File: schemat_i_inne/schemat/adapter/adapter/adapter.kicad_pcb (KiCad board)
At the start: 2 copper layers, 27.9 x 19 mm, 2 parts, among them J1 Conn_01x06_Female, J2 RJ45

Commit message: Upraszczanie polaczen i poprawianie plytki
Gotowe polaczenia do ekranu
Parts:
- added C1: C, Connector_PinHeader_2.54mm:PinHeader_1x02_P2.54mm_Vertical, F.Cu at (34.3, 20.3)
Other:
- board size 27.9 x 19 mm -> 186.7 x 274.3 mm
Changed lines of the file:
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@@
   (general
     (thickness 1.6)
-    (drawings 4)
+    (drawings 6)
     (tracks 12)
     (zones 0)
-    (modules 2)
+    (modules 3)
     (nets 9)
   )
-  (page A4)
+  (page A4 portrait)
   (layers
     (0 F.Cu signal)
@@
   )
   (setup
-    (last_trace_width 0.5)
+    (last_trace_width 0.25)
     (user_trace_width 0.5)
     (user_trace_width 1)
@@
   (net 3 "Net-(J1-Pad4)")
   (net 4 "Net-(J1-Pad3)")
-  (net 5 "Net-(J1-Pad2)")
-  (net 6 "Net-(J1-Pad1)")
-  (net 7 "Net-(J2-Pad8)")
-  (net 8 "Net-(J2-Pad7)")
+  (net 5 "Net-(J2-Pad8)")
+  (net 6 "Net-(J2-Pad7)")
+  (net 7 "Net-(C1-Pad2)")
+  (net 8 "Net-(C1-Pad1)")
   (net_class Default "To jest domyślna klasa połączeń."
     (clearance 0.2)
@@
     (uvia_dia 0.3)
     (uvia_drill 0.1)
-    (add_net "Net-(J1-Pad1)")
-    (add_net "Net-(J1-Pad2)")
+    (add_net "Net-(C1-Pad1)")
+    (add_net "Net-(C1-Pad2)")
     (add_net "Net-(J1-Pad3)")
     (add_net "Net-(J1-Pad4)")
@@
     (add_net "Net-(J2-Pad7)")
     (add_net "Net-(J2-Pad8)")
+  )
+  (module Connector_PinHeader_2.54mm:PinHeader_1x02_P2.54mm_Vertical (layer F.Cu)
+    (at 34.29 20.32)
+    (descr "Through hole straight pin header, 1x02, 2.54mm pitch, single row")
+    (tags "Through hole pin header THT 1x02 2.54mm single row")
+    (fp_text reference C1 (at 0 -2.33) (layer F.SilkS)
+      (effects (font (size 1 1) (thickness 0.15)))
+    )
+    (fp_text value C (at 0 4.87) (layer F.Fab)
+      (effects (font (size 1 1) (thickness 0.15)))
+    )
+    (fp_text user %R (at 0 1.27 90) (layer F.Fab)
+      (effects (font (size 1 1) (thickness 0.15)))
+    )
+    (fp_line (start 1.8 -1.8) (end -1.8 -1.8) (layer F.CrtYd) (width 0.05))
+    (fp_line (start 1.8 4.35) (end 1.8 -1.8) (layer F.CrtYd) (width 0.05))
+    (fp_line (start -1.8 4.35) (end 1.8 4.35) (layer F.CrtYd) (width 0.05))
+    (fp_line (start -1.8 -1.8) (end -1.8 4.35) (layer F.CrtYd) (width 0.05))
+    (fp_line (start -1.33 -1.33) (end 0 -1.33) (layer F.SilkS) (width 0.12))
+    (fp_line (start -1.33 0) (end -1.33 -1.33) (layer F.SilkS) (width 0.12))
+    (fp_line (start -1.33 1.27) (end 1.33 1.27) (layer F.SilkS) (width 0.12))
+    (fp_line (start 1.33 1.27) (end 1.33 3.87) (layer F.SilkS) (width 0.12))
+    (fp_line (start -1.33 1.27) (end -1.33 3.87) (layer F.SilkS) (width 0.12))
+    (fp_line (start -1.33 3.87) (end 1.33 3.87) (layer F.SilkS) (width 0.12))
+    (fp_line (start -1.27 -0.635) (end -0.635 -1.27) (layer F.Fab) (width 0.1))
+    (fp_line (start -1.27 3.81) (end -1.27 -0.635) (layer F.Fab) (width 0.1))
+    (fp_line (start 1.27 3.81) (end -1.27 3.81) (layer F.Fab) (width 0.1))
+    (fp_line (start 1.27 -1.27) (end 1.27 3.81) (layer F.Fab) (width 0.1))
+    (fp_line (start -0.635 -1.27) (end 1.27 -1.27) (layer F.Fab) (width 0.1))
+    (pad 2 thru_hole oval (at 0 2.54) (size 1.7 1.7) (drill 1) (layers *.Cu *.Mask)
+      (net 7 "Net-(C1-Pad2)"))
+    (pad 1 thru_hole rect (at 0 0) (size 1.7 1.7) (drill 1) (layers *.Cu *.Mask)
+      (net 8 "Net-(C1-Pad1)"))
+    (model ${KISYS3DMOD}/Connector_PinHeader_2.54mm.3dshapes/PinHeader_1x02_P2.54mm_Vertical.wrl
+      (at (xyz 0 0 0))
+      (scale (xyz 1 1 1))
+      (rotate (xyz 0 0 0))
+    )
   )
   (module Connector_RJ:RJ45_Amphenol_54602-x08_Horizontal (layer F.Cu)
@@
     )
     (pad 8 thru_hole circle (at 8.89 -2.54 270) (size 1.5 1.5) (drill 0.76) (layers *.Cu *.Mask)
-      (net 7 "Net-(J2-Pad8)"))
+      (net 5 "Net-(J2-Pad8)"))
     (pad 7 thru_hole circle (at 7.62 0 270) (size 1.5 1.5) (drill 0.76) (layers *.Cu *.Mask)
-      (net 8 "Net-(J2-Pad7)"))
+      (net 6 "Net-(J2-Pad7)"))
     (pad 6 thru_hole circle (at 6.35 -2.54 270) (size 1.5 1.5) (drill 0.76) (layers *.Cu *.Mask)
       (net 1 "Net-(J1-Pad6)"))
@@
       (net 4 "Net-(J1-Pad3)"))
     (pad 2 thru_hole circle (at 1.27 -2.54 270) (size 1.5 1.5) (drill 0.76) (layers *.Cu *.Mask)
-      (net 5 "Net-(J1-Pad2)"))
+      (net 7 "Net-(C1-Pad2)"))
     (pad 1 thru_hole rect (at 0 0 270) (size 1.5 1.5) (drill 0.76) (layers *.Cu *.Mask)
-      (net 6 "Net-(J1-Pad1)"))
+      (net 8 "Net-(C1-Pad1)"))
     (pad "" np_thru_hole circle (at -1.27 6.35 270) (size 3.2 3.2) (drill 3.2) (layers *.Cu *.Mask))
     (pad "" np_thru_hole circle (at 10.16 6.35 270) (size 3.2 3.2) (drill 3.2) (layers *.Cu *.Mask))
@@
       (net 4 "Net-(J1-Pad3)"))
     (pad 2 thru_hole oval (at 0 2.54) (size 1.7 1.7) (drill 1) (layers *.Cu *.Mask)
-      (net 5 "Net-(J1-Pad2)"))
+      (net 7 "Net-(C1-Pad2)"))
     (pad 1 thru_hole rect (at 0 0) (size 1.7 1.7) (drill 1) (layers *.Cu *.Mask)
-      (net 6 "Net-(J1-Pad1)"))
+      (net 8 "Net-(C1-Pad1)"))
     (model ${KISYS3DMOD}/Connector_PinHeader_2.54mm.3dshapes/PinHeader_1x06_P2.54mm_Vertical.wrl
       (at (xyz 0 0 0))
@@
     )
   )
-  (gr_line (start 40.64 17.78) (end 12.7 17.78) (layer Edge.Cuts) (width 0.05))
-  (gr_line (start 40.64 36.83) (end 40.64 17.78) (layer Edge.Cuts) (width 0.05))
-  (gr_line (start 12.7 36.83) (end 40.64 36.83) (layer Edge.Cuts) (width 0.05))
-  (gr_line (start 12.7 17.78) (end 12.7 36.83) (layer Edge.Cuts) (width 0.05))
+  (dimension 19.05 (width 0.12) (layer F.SilkS)
+    (gr_text "19,050 mm" (at 44.45 27.305 270) (layer F.SilkS)
+      (effects (font (size 1 1) (thickness 0.15)))
+    )
+    (feature1 (pts (xy 40.64 36.83) (xy 43.766421 36.83)))
+    (feature2 (pts (xy 40.64 17.78) (xy 43.766421 17.78)))
+    (crossbar (pts (xy 43.18 17.78) (xy 43.18 36.83)))
+    (arrow1a (pts (xy 43.18 36.83) (xy 42.593579 35.703496)))
+    (arrow1b (pts (xy 43.18 36.83) (xy 43.766421 35.703496)))
+    (arrow2a (pts (xy 43.18 17.78) (xy 42.593579 18.906504)))
+    (arrow2b (pts (xy 43.18 17.78) (xy 43.766421 18.906504)))
+  )
+  (dimension 27.94 (width 0.12) (layer F.SilkS)
+    (gr_text "27,940 mm" (at 26.67 15.24) (layer F.SilkS)
+      (effects (font (size 1 1) (thickness 0.15)))
+    )
+    (feature1 (pts (xy 40.64 17.78) (xy 40.64 15.923579)))
+    (feature2 (pts (xy 12.7 17.78) (xy 12.7 15.923579)))
+    (crossbar (pts (xy 12.7 16.51) (xy 40.64 16.51)))
+    (arrow1a (pts (xy 40.64 16.51) (xy 39.513496 17.096421)))
+    (arrow1b (pts (xy 40.64 16.51) (xy 39.513496 15.923579)))
+    (arrow2a (pts (xy 12.7 16.51) (xy 13.826504 17.096421)))
+    (arrow2b (pts (xy 12.7 16.51) (xy 13.826504 15.923579)))
+  )
+  (gr_line (start 11.43 285.75) (end 11.43 11.43) (layer Edge.Cuts) (width 0.05))
+  (gr_line (start 198.12 285.75) (end 11.43 285.75) (layer Edge.Cuts) (width 0.05))
+  (gr_line (start 198.12 11.43) (end 198.12 285.75) (layer Edge.Cuts) (width 0.05))
+  (gr_line (start 11.43 11.43) (end 198.12 11.43) (layer Edge.Cuts) (width 0.05))
   (segment (start 34.29 29.21) (end 38.1 33.02) (width 0.25) (layer F.Cu) (net 1))
   (segment (start 30.48 29.21) (end 34.29 29.21) (width 0.25) (layer F.Cu) (net 1))
@@
   (segment (start 30.48 26.67) (end 36.83 26.67) (width 0.25) (layer F.Cu) (net 3))
   (segment (start 27.94 25.4) (end 38.1 25.4) (width 0.25) (layer F.Cu) (net 4))
-  (segment (start 31.75 22.86) (end 30.48 24.13) (width 0.5) (layer F.Cu) (net 5))
-  (segment (start 38.1 22.86) (end 31.75 22.86) (width 0.5) (layer F.Cu) (net 5))
-  (segment (start 27.94 21.61) (end 27.94 22.86) (width 0.5) (layer F.Cu) (net 6))
-  (segment (start 29.23 20.32) (end 27.94 21.61) (width 0.5) (layer F.Cu) (net 6))
-  (segment (start 38.1 20.32) (end 29.23 20.32) (width 0.5) (layer F.Cu) (net 6))
-  (zone (net 5) (net_name "Net-(J1-Pad2)") (layer F.Cu) (hatch edge 0.508)
+  (segment (start 31.75 22.86) (end 30.48 24.13) (width 0.5) (layer F.Cu) (net 7))
+  (segment (start 38.1 22.86) (end 31.75 22.86) (width 0.5) (layer F.Cu) (net 7))
+  (segment (start 27.94 21.61) (end 27.94 22.86) (width 0.5) (layer F.Cu) (net 8))
+  (segment (start 29.23 20.32) (end 27.94 21.61) (width 0.5) (layer F.Cu) (net 8))
+  (segment (start 38.1 20.32) (end 29.23 20.32) (width 0.5) (layer F.Cu) (net 8))
+  (zone (net 7) (net_name "Net-(C1-Pad2)") (layer F.Cu) (hatch edge 0.508)
     (connect_pads yes (clearance 0.508))
     (min_thickness 0.254)

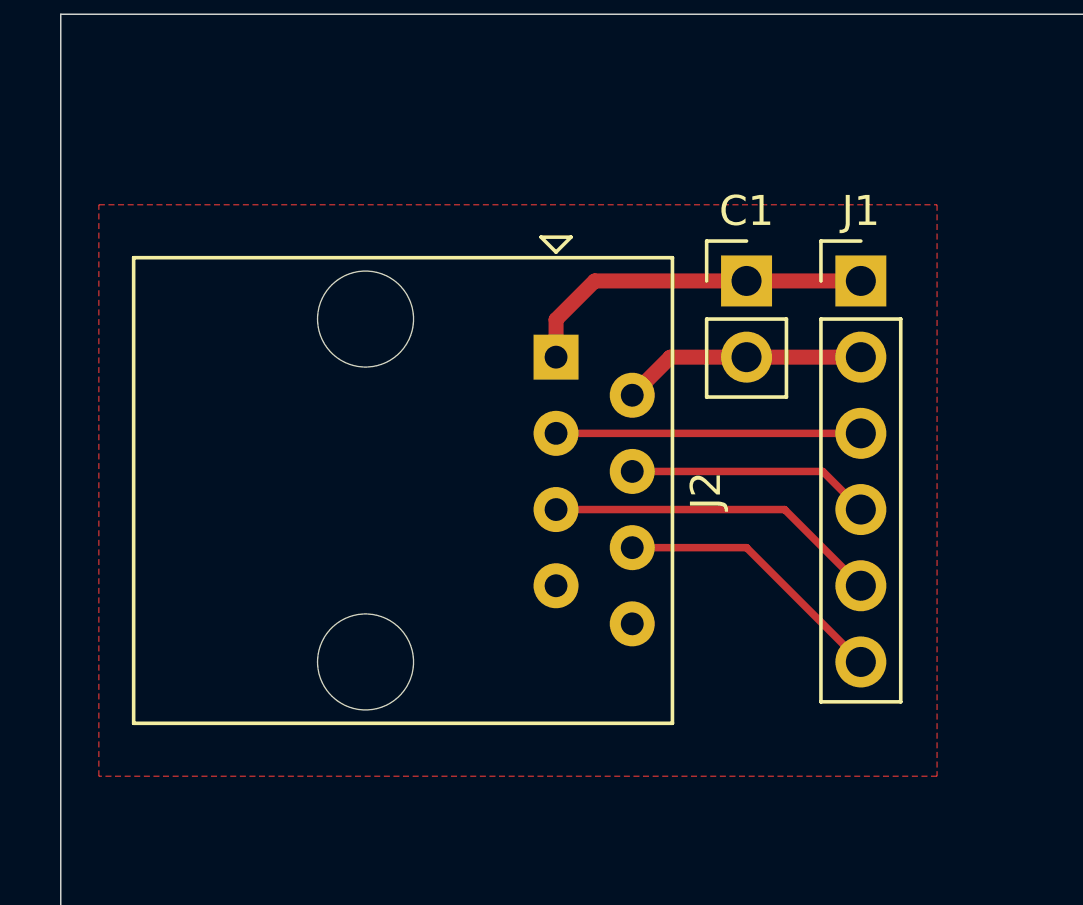
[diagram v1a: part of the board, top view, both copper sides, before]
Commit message: Koncowe sciezki i adapter
Ukonczono poprawianie sciezek i poprawnie zrobiono adapter
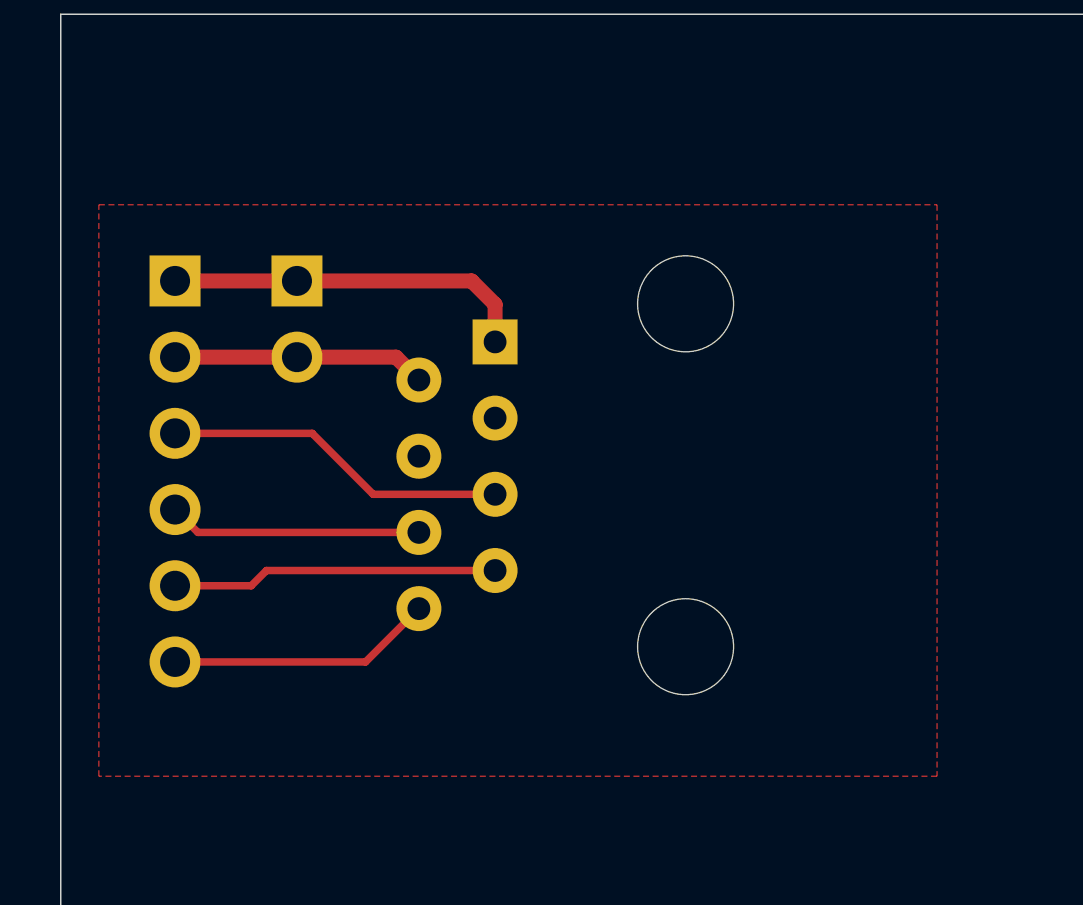
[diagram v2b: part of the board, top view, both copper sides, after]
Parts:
- C1, J1, J2: moved to B.Cu
- moved J1 22.9 mm to (15.2, 20.3), turned to 180 degrees
- moved C1 15.0 mm to (19.3, 20.3), turned to 180 degrees
- moved J2 2.09 mm to (25.9, 22.4)
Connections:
- J2 pad 3: Net-(J1-Pad3) -> Net-(J2-Pad3)
- J2 pad 4: Net-(J1-Pad4) -> Net-(J2-Pad4)
- J2 pad 5: Net-(J1-Pad5) -> Net-(J1-Pad3)
- J2 pad 6: Net-(J1-Pad6) -> Net-(J1-Pad4)
- J2 pad 7: Net-(J2-Pad7) -> Net-(J1-Pad5)
- J2 pad 8: Net-(J2-Pad8) -> Net-(J1-Pad6)
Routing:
- net Net-(J1-Pad3): track 10.2 -> 11.5 mm

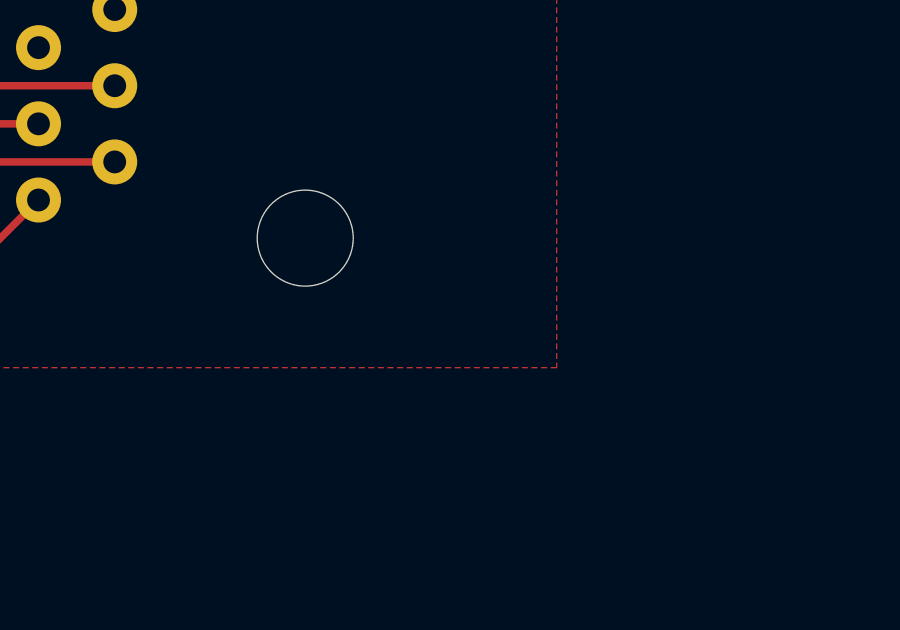
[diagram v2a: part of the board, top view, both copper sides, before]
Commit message: Logo i wymiary
Dodano "by KK" i wymiary plyty glownej
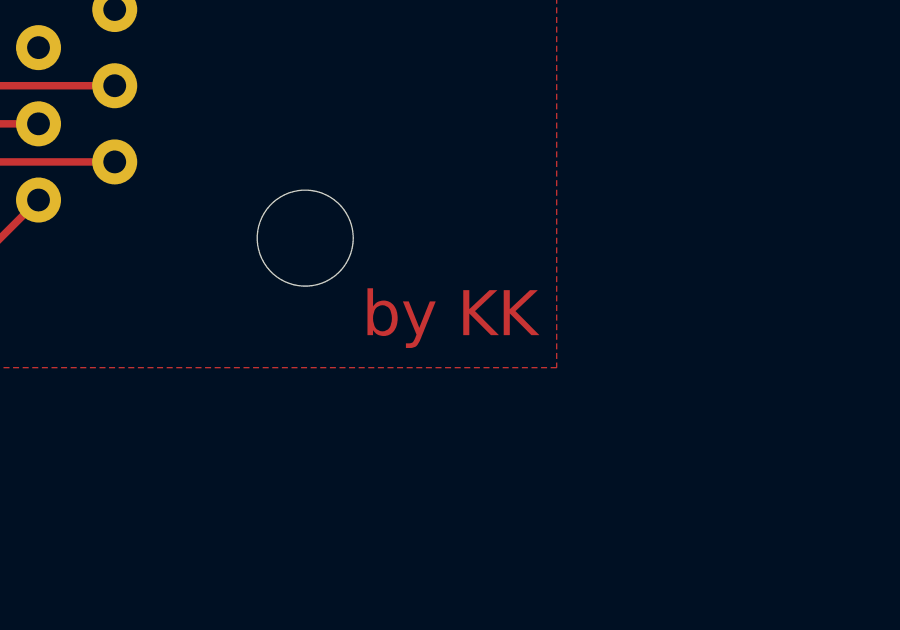
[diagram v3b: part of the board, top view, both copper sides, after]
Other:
- board text added: "by KK"
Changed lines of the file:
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@@
   (general
     (thickness 1.6)
-    (drawings 6)
+    (drawings 7)
     (tracks 18)
     (zones 0)
@@
     )
   )
+  (gr_text "by KK" (at 37.084 35.052) (layer F.Cu)
+    (effects (font (size 1.5 1.5) (thickness 0.3)))
+  )
   (dimension 19.05 (width 0.12) (layer F.SilkS)

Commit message: Working CMake build and upload
use following comands
./configure.sh
./build.sh
./upload.sh
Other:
- net class Default removed
